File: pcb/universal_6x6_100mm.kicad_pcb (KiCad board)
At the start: 2 copper layers, 100 x 100 mm, 80 parts

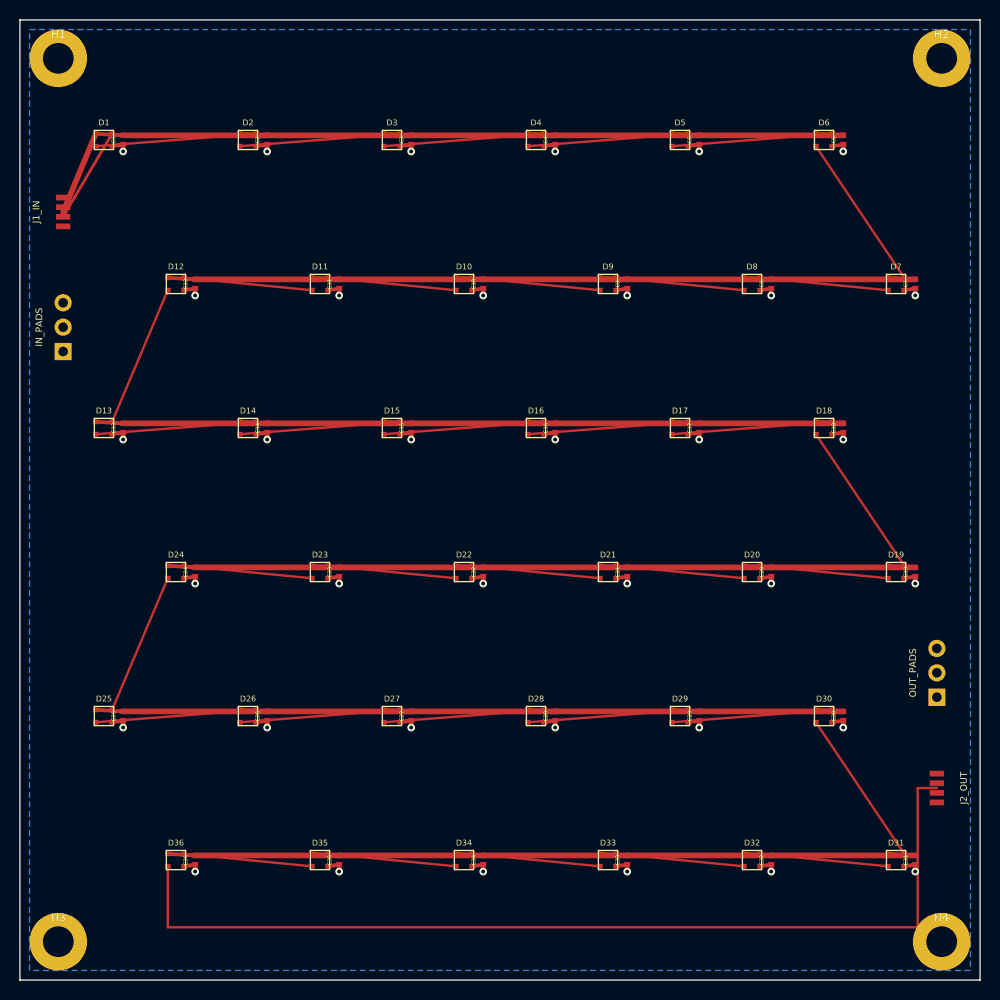
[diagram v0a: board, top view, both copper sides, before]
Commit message: feat: implement seamless 17mm pitch and 4-edge JST-PH ports for 6x6 matrix
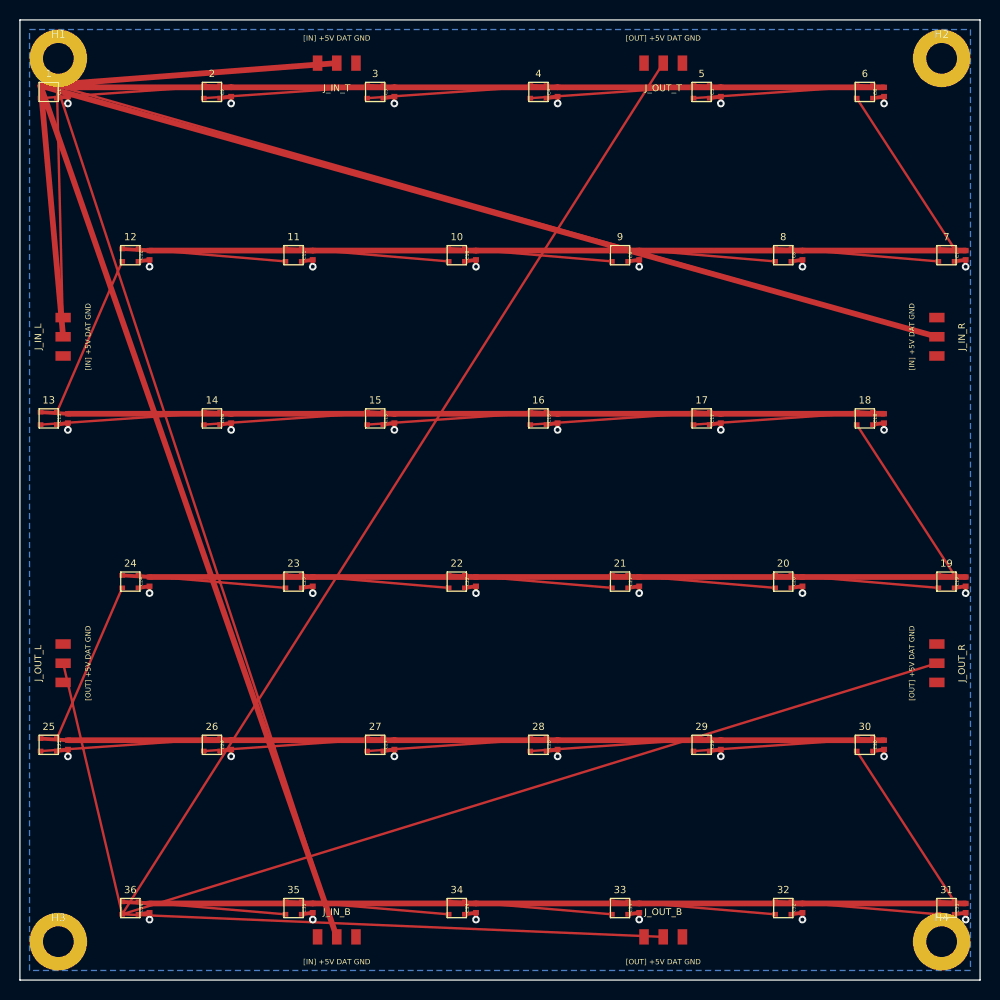
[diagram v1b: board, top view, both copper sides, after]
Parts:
- removed D1, D10, D11, D12, D13, D14, D15, D16, D17, D18, D19, D2, D20, D21, D22, D23, D24, D25, D26, D27, D28, D29, D3, D30, D31, D32, D33, D34, D35, D36, D4, D5, D6, D7, D8, D9: , LED_SMD:LED_WS2812B_PLCC4_2.0x2.0mm
- removed IN_PADS, OUT_PADS: , Connector_PinHeader_2.54mm:PinHeader_1x03_P2.54mm_Vertical
- removed J1_IN, J2_OUT: , Connector_FFC-FPC:Molex_200528-0040_1x04-1MP_P1.00mm_Horizontal
- added 1: , LED_SMD:LED_WS2812B_PLCC4_2.0x2.0mm, F.Cu at (3.00, 7.50)
- added 10: , LED_SMD:LED_WS2812B_PLCC4_2.0x2.0mm, F.Cu at (45.5, 24.5)
- added 11: , LED_SMD:LED_WS2812B_PLCC4_2.0x2.0mm, F.Cu at (28.5, 24.5)
- added 12: , LED_SMD:LED_WS2812B_PLCC4_2.0x2.0mm, F.Cu at (11.5, 24.5)
- added 13: , LED_SMD:LED_WS2812B_PLCC4_2.0x2.0mm, F.Cu at (3.00, 41.5)
- added 14: , LED_SMD:LED_WS2812B_PLCC4_2.0x2.0mm, F.Cu at (20.0, 41.5)
- added 15: , LED_SMD:LED_WS2812B_PLCC4_2.0x2.0mm, F.Cu at (37.0, 41.5)
- added 16: , LED_SMD:LED_WS2812B_PLCC4_2.0x2.0mm, F.Cu at (54.0, 41.5)
- added 17: , LED_SMD:LED_WS2812B_PLCC4_2.0x2.0mm, F.Cu at (71.0, 41.5)
- added 18: , LED_SMD:LED_WS2812B_PLCC4_2.0x2.0mm, F.Cu at (88.0, 41.5)
- added 19: , LED_SMD:LED_WS2812B_PLCC4_2.0x2.0mm, F.Cu at (96.5, 58.5)
- added 2: , LED_SMD:LED_WS2812B_PLCC4_2.0x2.0mm, F.Cu at (20.0, 7.50)
- added 20: , LED_SMD:LED_WS2812B_PLCC4_2.0x2.0mm, F.Cu at (79.5, 58.5)
- added 21: , LED_SMD:LED_WS2812B_PLCC4_2.0x2.0mm, F.Cu at (62.5, 58.5)
- added 22: , LED_SMD:LED_WS2812B_PLCC4_2.0x2.0mm, F.Cu at (45.5, 58.5)
- added 23: , LED_SMD:LED_WS2812B_PLCC4_2.0x2.0mm, F.Cu at (28.5, 58.5)
- added 24: , LED_SMD:LED_WS2812B_PLCC4_2.0x2.0mm, F.Cu at (11.5, 58.5)
- added 25: , LED_SMD:LED_WS2812B_PLCC4_2.0x2.0mm, F.Cu at (3.00, 75.5)
- added 26: , LED_SMD:LED_WS2812B_PLCC4_2.0x2.0mm, F.Cu at (20.0, 75.5)
- added 27: , LED_SMD:LED_WS2812B_PLCC4_2.0x2.0mm, F.Cu at (37.0, 75.5)
- added 28: , LED_SMD:LED_WS2812B_PLCC4_2.0x2.0mm, F.Cu at (54.0, 75.5)
- added 29: , LED_SMD:LED_WS2812B_PLCC4_2.0x2.0mm, F.Cu at (71.0, 75.5)
- added 3: , LED_SMD:LED_WS2812B_PLCC4_2.0x2.0mm, F.Cu at (37.0, 7.50)
- added 30: , LED_SMD:LED_WS2812B_PLCC4_2.0x2.0mm, F.Cu at (88.0, 75.5)
- added 31: , LED_SMD:LED_WS2812B_PLCC4_2.0x2.0mm, F.Cu at (96.5, 92.5)
- added 32: , LED_SMD:LED_WS2812B_PLCC4_2.0x2.0mm, F.Cu at (79.5, 92.5)
- added 33: , LED_SMD:LED_WS2812B_PLCC4_2.0x2.0mm, F.Cu at (62.5, 92.5)
- added 34: , LED_SMD:LED_WS2812B_PLCC4_2.0x2.0mm, F.Cu at (45.5, 92.5)
- added 35: , LED_SMD:LED_WS2812B_PLCC4_2.0x2.0mm, F.Cu at (28.5, 92.5)
- added 36: , LED_SMD:LED_WS2812B_PLCC4_2.0x2.0mm, F.Cu at (11.5, 92.5)
- added 4: , LED_SMD:LED_WS2812B_PLCC4_2.0x2.0mm, F.Cu at (54.0, 7.50)
- added 5: , LED_SMD:LED_WS2812B_PLCC4_2.0x2.0mm, F.Cu at (71.0, 7.50)
- added 6: , LED_SMD:LED_WS2812B_PLCC4_2.0x2.0mm, F.Cu at (88.0, 7.50)
- added 7: , LED_SMD:LED_WS2812B_PLCC4_2.0x2.0mm, F.Cu at (96.5, 24.5)
- added 8: , LED_SMD:LED_WS2812B_PLCC4_2.0x2.0mm, F.Cu at (79.5, 24.5)
- added 9: , LED_SMD:LED_WS2812B_PLCC4_2.0x2.0mm, F.Cu at (62.5, 24.5)
- added J_IN_B: , Connector_JST:JST_PH_S3B-PH-SM4-TB_1x03-1MP_P2.00mm_Horizontal, F.Cu at (33.0, 95.5)
- added J_IN_L: , Connector_JST:JST_PH_S3B-PH-SM4-TB_1x03-1MP_P2.00mm_Horizontal, F.Cu at (4.50, 33.0)
- added J_IN_R: , Connector_JST:JST_PH_S3B-PH-SM4-TB_1x03-1MP_P2.00mm_Horizontal, F.Cu at (95.5, 33.0)
- added J_IN_T: , Connector_JST:JST_PH_S3B-PH-SM4-TB_1x03-1MP_P2.00mm_Horizontal, F.Cu at (33.0, 4.50)
- added J_OUT_B: , Connector_JST:JST_PH_S3B-PH-SM4-TB_1x03-1MP_P2.00mm_Horizontal, F.Cu at (67.0, 95.5)
- added J_OUT_L: , Connector_JST:JST_PH_S3B-PH-SM4-TB_1x03-1MP_P2.00mm_Horizontal, F.Cu at (4.50, 67.0)
- added J_OUT_R: , Connector_JST:JST_PH_S3B-PH-SM4-TB_1x03-1MP_P2.00mm_Horizontal, F.Cu at (95.5, 67.0)
- added J_OUT_T: , Connector_JST:JST_PH_S3B-PH-SM4-TB_1x03-1MP_P2.00mm_Horizontal, F.Cu at (67.0, 4.50)
- moved C1 7.62 mm to (5.00, 7.50)
- moved C31 7.25 mm to (98.5, 92.5)
- moved C36 6.90 mm to (13.5, 92.5)
- moved C6 6.56 mm to (90.0, 7.50)
- moved C25 6.49 mm to (5.00, 75.5)
- moved C2 6.25 mm to (22.0, 7.50)
- moved C7 6.05 mm to (98.5, 24.5)
- moved C32 5.96 mm to (81.5, 92.5)
- moved C13 5.84 mm to (5.00, 41.5)
- moved C35 5.71 mm to (30.5, 92.5)
- moved C12 5.62 mm to (13.5, 24.5)
- moved C5 5.48 mm to (73.0, 7.50)
- moved C19 5.34 mm to (98.5, 58.5)
- moved C3 5.30 mm to (39.0, 7.50)
- moved C30 5.20 mm to (90.0, 75.5)
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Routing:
- net +5V: track 561.6 -> 860.8 mm
- net DATA_1: track 10.0 -> 244.0 mm
- net DATA_37: track 100.9 -> 277.1 mm
- net DATA_25: track 14.9 -> 17.1 mm
- net DATA_13: track 14.9 -> 17.1 mm
- net DATA_19: track 16.5 -> 18.7 mm
- net DATA_7: track 16.5 -> 18.7 mm
- net DATA_31: track 16.5 -> 18.7 mm
- net DATA_6: track 16.8 -> 18.7 mm
- net DATA_5: track 16.8 -> 18.7 mm
- net DATA_4: track 16.8 -> 18.7 mm
- net DATA_30: track 16.8 -> 18.7 mm
- net DATA_3: track 16.8 -> 18.7 mm
- net DATA_29: track 16.8 -> 18.7 mm
- net DATA_28: track 16.8 -> 18.7 mm
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
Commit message: feat: add corner M3 mounting holes, fabric sewing eyelets, and auto-match BOM C3029441
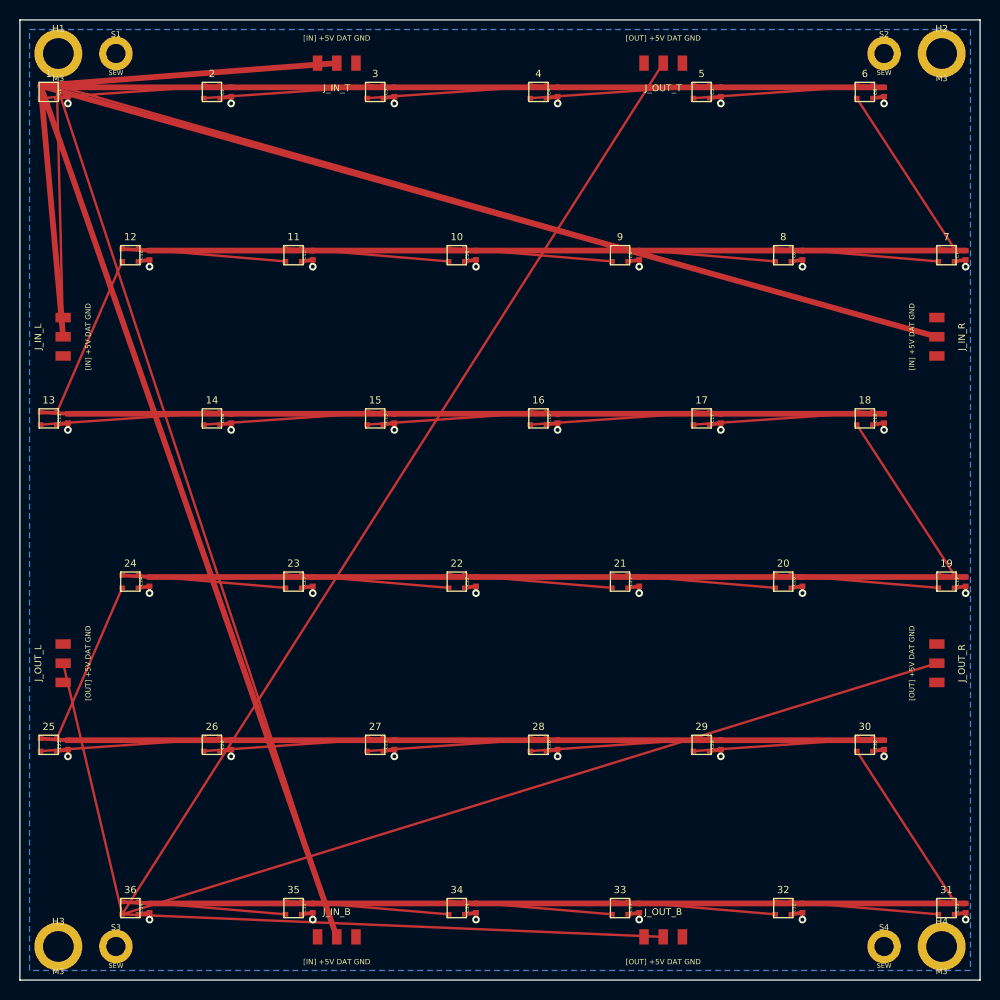
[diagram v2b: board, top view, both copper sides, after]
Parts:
- added S1: , MountingHole:MountingHole_2.0mm, F.Cu at (10.0, 3.50)
- added S2: , MountingHole:MountingHole_2.0mm, F.Cu at (90.0, 3.50)
- added S3: , MountingHole:MountingHole_2.0mm, F.Cu at (10.0, 96.5)
- added S4: , MountingHole:MountingHole_2.0mm, F.Cu at (90.0, 96.5)
- moved H1 0.50 mm to (4.00, 3.50)
- moved H2 0.50 mm to (96.0, 3.50)
- moved H3 0.50 mm to (4.00, 96.5)
- moved H4 0.50 mm to (96.0, 96.5)
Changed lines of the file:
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@@
     (tracks 0)
     (zones 0)
-    (modules 84)
+    (modules 88)
     (nets 39)
   )
@@
   (gr_line (start 0 100.0) (end 0 0) (layer Edge.Cuts) (width 0.15))
   (module "MountingHole:MountingHole_3.2mm_M3" (layer F.Cu)
-    (at 4.0 4.0)
+    (at 4.0 3.5)
     (descr "Mounting Hole 3.2mm M3")
-    (path "/hole_1")
-    (fp_text reference "H1" (at 0 -2.5) (layer F.SilkS)
-      (effects (font (size 0.8 0.8) (thickness 0.15)))
+    (path "/H1")
+    (fp_text reference "H1" (at 0 -2.6) (layer F.SilkS)
+      (effects (font (size 0.7 0.7) (thickness 0.12)))
     )
-    (pad 1 thru_hole circle (at 0 0) (size 6.0 6.0) (drill 3.2) (layers *.Cu *.Mask))
+    (fp_text user "M3" (at 0 2.6) (layer F.SilkS)
+      (effects (font (size 0.6 0.6) (thickness 0.1)))
+    )
+    (pad 1 thru_hole circle (at 0 0) (size 5.0 5.0) (drill 3.2) (layers *.Cu *.Mask))
   )
   (module "MountingHole:MountingHole_3.2mm_M3" (layer F.Cu)
-    (at 96.0 4.0)
+    (at 96.0 3.5)
     (descr "Mounting Hole 3.2mm M3")
-    (path "/hole_2")
-    (fp_text reference "H2" (at 0 -2.5) (layer F.SilkS)
-      (effects (font (size 0.8 0.8) (thickness 0.15)))
+    (path "/H2")
+    (fp_text reference "H2" (at 0 -2.6) (layer F.SilkS)
+      (effects (font (size 0.7 0.7) (thickness 0.12)))
     )
-    (pad 1 thru_hole circle (at 0 0) (size 6.0 6.0) (drill 3.2) (layers *.Cu *.Mask))
+    (fp_text user "M3" (at 0 2.6) (layer F.SilkS)
+      (effects (font (size 0.6 0.6) (thickness 0.1)))
+    )
+    (pad 1 thru_hole circle (at 0 0) (size 5.0 5.0) (drill 3.2) (layers *.Cu *.Mask))
   )
   (module "MountingHole:MountingHole_3.2mm_M3" (layer F.Cu)
-    (at 4.0 96.0)
+    (at 4.0 96.5)
     (descr "Mounting Hole 3.2mm M3")
-    (path "/hole_3")
-    (fp_text reference "H3" (at 0 -2.5) (layer F.SilkS)
-      (effects (font (size 0.8 0.8) (thickness 0.15)))
+    (path "/H3")
+    (fp_text reference "H3" (at 0 -2.6) (layer F.SilkS)
+      (effects (font (size 0.7 0.7) (thickness 0.12)))
     )
-    (pad 1 thru_hole circle (at 0 0) (size 6.0 6.0) (drill 3.2) (layers *.Cu *.Mask))
+    (fp_text user "M3" (at 0 2.6) (layer F.SilkS)
+      (effects (font (size 0.6 0.6) (thickness 0.1)))
+    )
+    (pad 1 thru_hole circle (at 0 0) (size 5.0 5.0) (drill 3.2) (layers *.Cu *.Mask))
   )
   (module "MountingHole:MountingHole_3.2mm_M3" (layer F.Cu)
-    (at 96.0 96.0)
+    (at 96.0 96.5)
     (descr "Mounting Hole 3.2mm M3")
-    (path "/hole_4")
-    (fp_text reference "H4" (at 0 -2.5) (layer F.SilkS)
-      (effects (font (size 0.8 0.8) (thickness 0.15)))
+    (path "/H4")
+    (fp_text reference "H4" (at 0 -2.6) (layer F.SilkS)
+      (effects (font (size 0.7 0.7) (thickness 0.12)))
     )
-    (pad 1 thru_hole circle (at 0 0) (size 6.0 6.0) (drill 3.2) (layers *.Cu *.Mask))
+    (fp_text user "M3" (at 0 2.6) (layer F.SilkS)
+      (effects (font (size 0.6 0.6) (thickness 0.1)))
+    )
+    (pad 1 thru_hole circle (at 0 0) (size 5.0 5.0) (drill 3.2) (layers *.Cu *.Mask))
+  )
+  (module "MountingHole:MountingHole_2.0mm" (layer F.Cu)
+    (at 10.0 3.5)
+    (descr "Fabric Sewing Eyelet 2.0mm")
+    (path "/S1")
+    (fp_text reference "S1" (at 0 -2.0) (layer F.SilkS)
+      (effects (font (size 0.6 0.6) (thickness 0.1)))
+    )
+    (fp_text user "SEW" (at 0 2.0) (layer F.SilkS)
+      (effects (font (size 0.5 0.5) (thickness 0.08)))
+    )
+    (pad 1 thru_hole circle (at 0 0) (size 3.5 3.5) (drill 2.0) (layers *.Cu *.Mask))
+  )
+  (module "MountingHole:MountingHole_2.0mm" (layer F.Cu)
+    (at 90.0 3.5)
+    (descr "Fabric Sewing Eyelet 2.0mm")
+    (path "/S2")
+    (fp_text reference "S2" (at 0 -2.0) (layer F.SilkS)
+      (effects (font (size 0.6 0.6) (thickness 0.1)))
+    )
+    (fp_text user "SEW" (at 0 2.0) (layer F.SilkS)
+      (effects (font (size 0.5 0.5) (thickness 0.08)))
+    )
+    (pad 1 thru_hole circle (at 0 0) (size 3.5 3.5) (drill 2.0) (layers *.Cu *.Mask))
+  )
+  (module "MountingHole:MountingHole_2.0mm" (layer F.Cu)
+    (at 10.0 96.5)
+    (descr "Fabric Sewing Eyelet 2.0mm")
+    (path "/S3")
+    (fp_text reference "S3" (at 0 -2.0) (layer F.SilkS)
+      (effects (font (size 0.6 0.6) (thickness 0.1)))
+    )
+    (fp_text user "SEW" (at 0 2.0) (layer F.SilkS)
+      (effects (font (size 0.5 0.5) (thickness 0.08)))
+    )
+    (pad 1 thru_hole circle (at 0 0) (size 3.5 3.5) (drill 2.0) (layers *.Cu *.Mask))
+  )
+  (module "MountingHole:MountingHole_2.0mm" (layer F.Cu)
+    (at 90.0 96.5)
+    (descr "Fabric Sewing Eyelet 2.0mm")
+    (path "/S4")
+    (fp_text reference "S4" (at 0 -2.0) (layer F.SilkS)
+      (effects (font (size 0.6 0.6) (thickness 0.1)))
+    )
+    (fp_text user "SEW" (at 0 2.0) (layer F.SilkS)
+      (effects (font (size 0.5 0.5) (thickness 0.08)))
+    )
+    (pad 1 thru_hole circle (at 0 0) (size 3.5 3.5) (drill 2.0) (layers *.Cu *.Mask))
   )
   (module "Connector_JST:JST_PH_S3B-PH-SM4-TB_1x03-1MP_P2.00mm_Horizontal" (layer F.Cu)

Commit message: feat: straight 3-wire JST port alignment, vector silkscreen pin markings, and on-board LED numbering
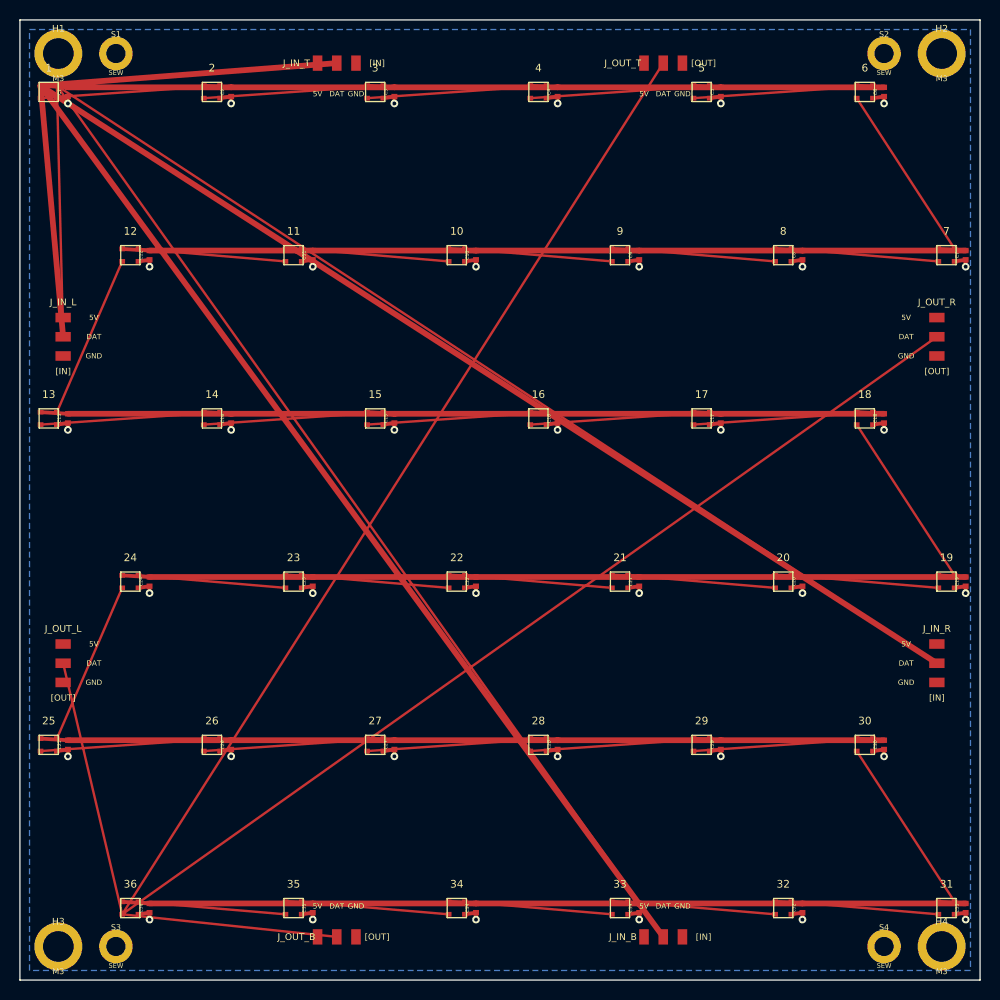
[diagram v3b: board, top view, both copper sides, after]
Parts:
- moved J_IN_B 34.0 mm to (67.0, 95.5)
- moved J_IN_R 34.0 mm to (95.5, 67.0), turned to 0 degrees
- moved J_OUT_B 34.0 mm to (33.0, 95.5)
- moved J_OUT_R 34.0 mm to (95.5, 33.0), turned to 0 degrees
- turned J_IN_L to 0 degrees
- turned J_IN_T to 0 degrees
- turned J_OUT_L to 0 degrees
- turned J_OUT_T to 0 degrees
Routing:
- net +5V: track 860.8 -> 890.9 mm
- net DATA_1: track 244.0 -> 273.9 mm
- net DATA_37: track 277.1 -> 258.4 mm
